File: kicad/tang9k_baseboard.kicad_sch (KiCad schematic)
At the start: 43 parts, among them J1 FPGA I/O, J2 FPGA I/O, J3 PMOD-FULL, J4 PMOD-FULL, J5 PMOD-FULL, J6 PMOD-HALF, J7 SERLED OUT, J8 FPGA I/O, J9 FPGA I/O, U1 SN74LV1T34DBV, U2 AP2205-18W5-7

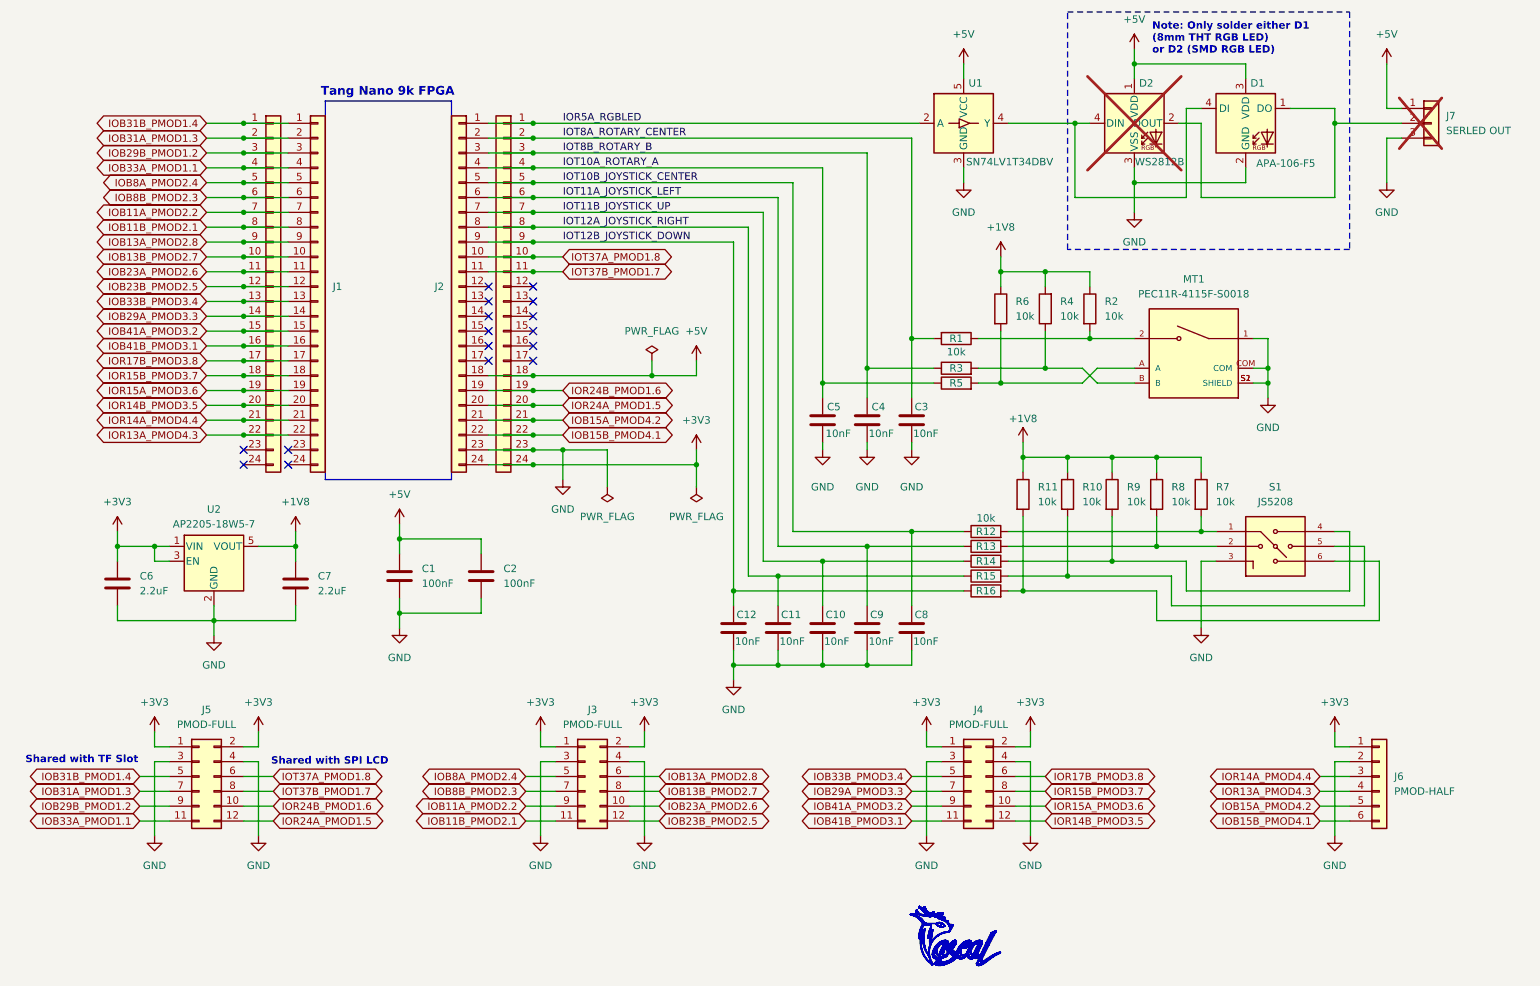
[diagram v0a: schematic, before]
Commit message: Fixed minor silkscreen issues
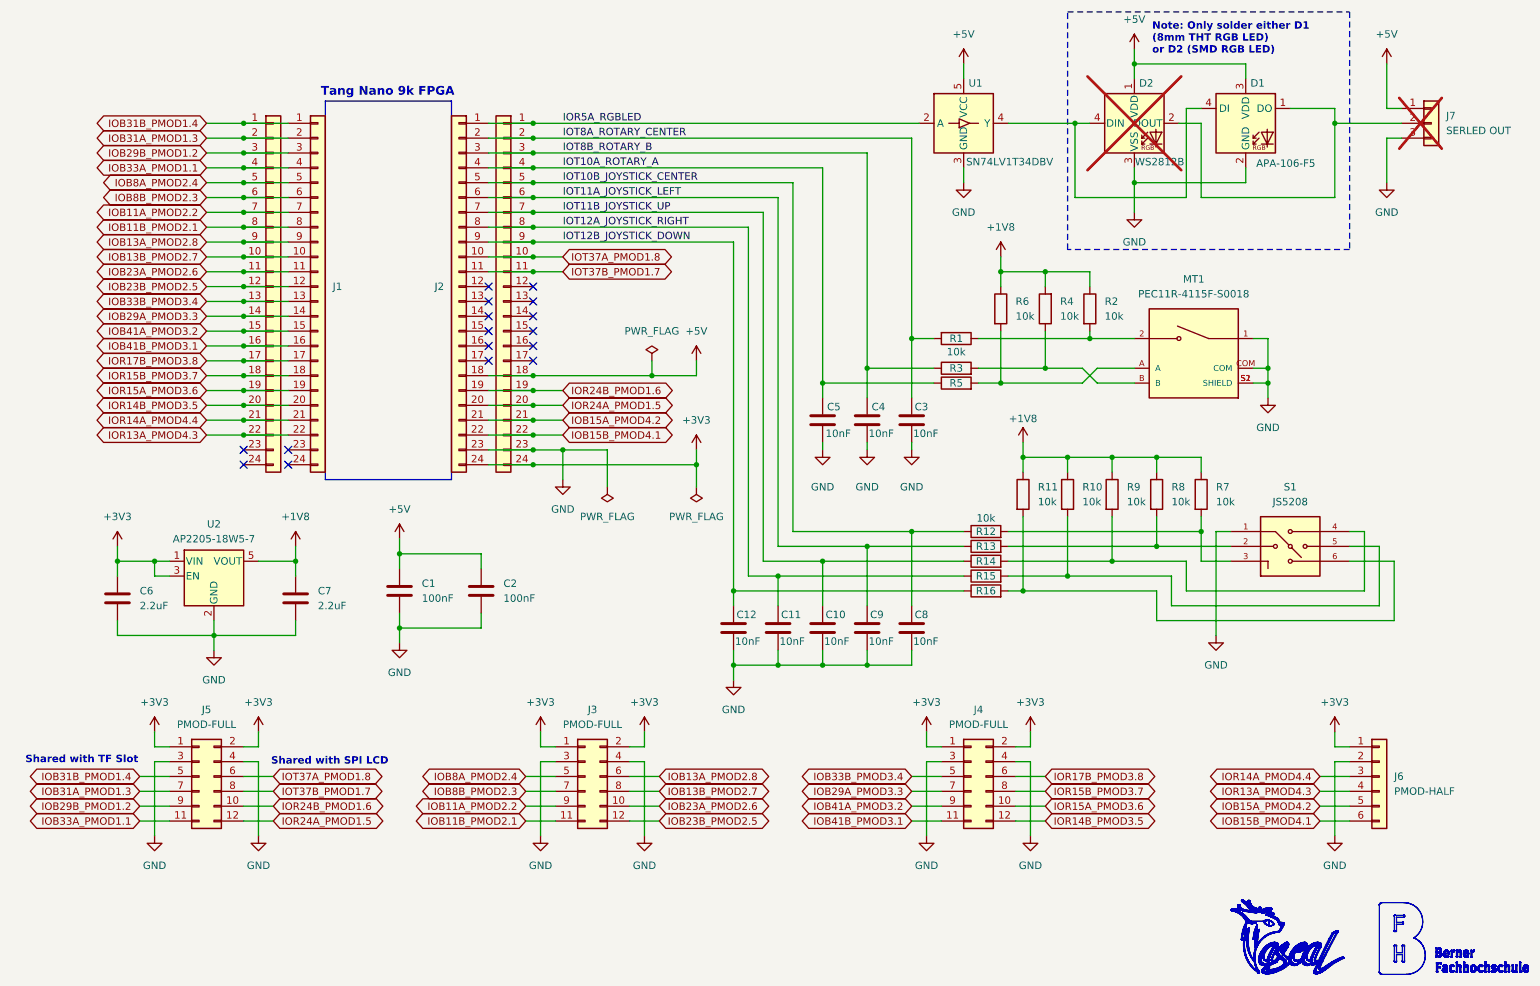
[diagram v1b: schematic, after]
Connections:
- net GND: now also S1.1; no longer S1.3
- net at R12.2, R7.2: now also S1.3; no longer S1.1
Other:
- company: Pascal G. (gfcwfzkm) -> Pascal G. (gesep1 / gfcwfzkm)
- moved on the sheet: C1, C2, C6, C7, S1, U2
